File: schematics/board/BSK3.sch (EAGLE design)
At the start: 44 parts

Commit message: Изменены площадки для сплавов Розе
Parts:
- U$15, U$16, U$6, U$7: value GRAFITGRAFIT3_1 -> GRAFITGRAFIT4_2; device CanCubeSat:GRAFITGRAFIT3_1 -> CanCubeSat:GRAFITGRAFIT4_2
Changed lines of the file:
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@@
 <part name="LED7" library="led" library_urn="urn:adsk.eagle:library:259" deviceset="LED" device="CHIPLED_0603" package3d_urn="urn:adsk.eagle:package:15822/2"/>
 <part name="R14" library="resistor" library_urn="urn:adsk.eagle:library:348" deviceset="R-US_" device="R0603" package3d_urn="urn:adsk.eagle:package:23555/3" value="1M"/>
-<part name="U$6" library="CanCubeSat" deviceset="GRAFIT" device="GRAFIT3_1"/>
-<part name="U$7" library="CanCubeSat" deviceset="GRAFIT" device="GRAFIT3_1"/>
-<part name="U$15" library="CanCubeSat" deviceset="GRAFIT" device="GRAFIT3_1"/>
-<part name="U$16" library="CanCubeSat" deviceset="GRAFIT" device="GRAFIT3_1"/>
+<part name="U$6" library="CanCubeSat" deviceset="GRAFIT" device="GRAFIT4_2" value="GRAFITGRAFIT4_2"/>
+<part name="U$7" library="CanCubeSat" deviceset="GRAFIT" device="GRAFIT4_2" value="GRAFITGRAFIT4_2"/>
+<part name="U$15" library="CanCubeSat" deviceset="GRAFIT" device="GRAFIT4_2" value="GRAFITGRAFIT4_2"/>
+<part name="U$16" library="CanCubeSat" deviceset="GRAFIT" device="GRAFIT4_2" value="GRAFITGRAFIT4_2"/>
 <part name="R75" library="rcl" library_urn="urn:adsk.eagle:library:334" deviceset="R-US_" device="R2512" package3d_urn="urn:adsk.eagle:package:23545/2" value="R01"/>
 <part name="R76" library="resistor" deviceset="R-US_" device="R0603" package3d_urn="urn:adsk.eagle:package:23555/3" value="10R"/>

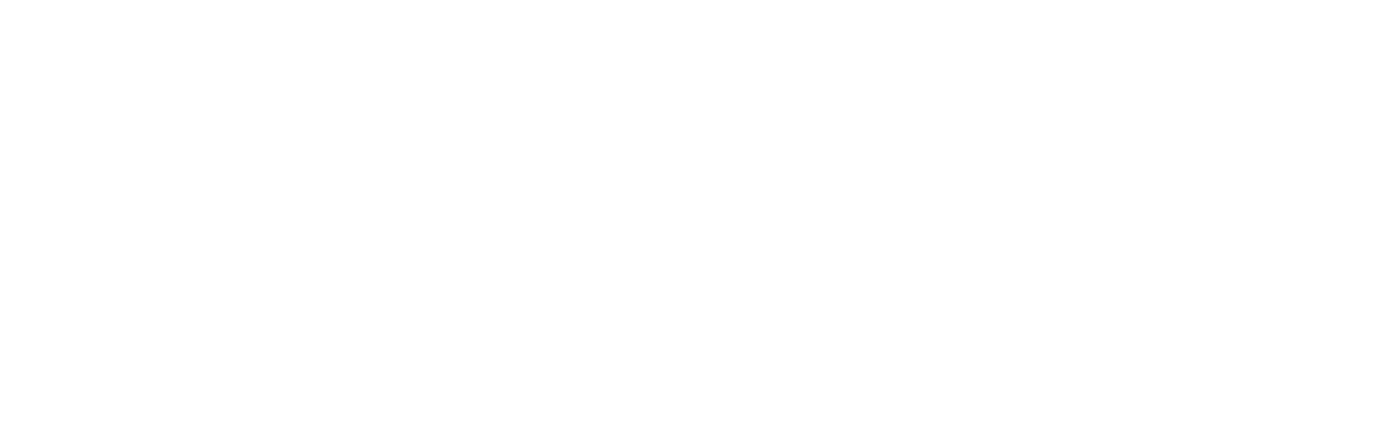
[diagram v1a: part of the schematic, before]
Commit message: Добавлены подписи Концерна к платам
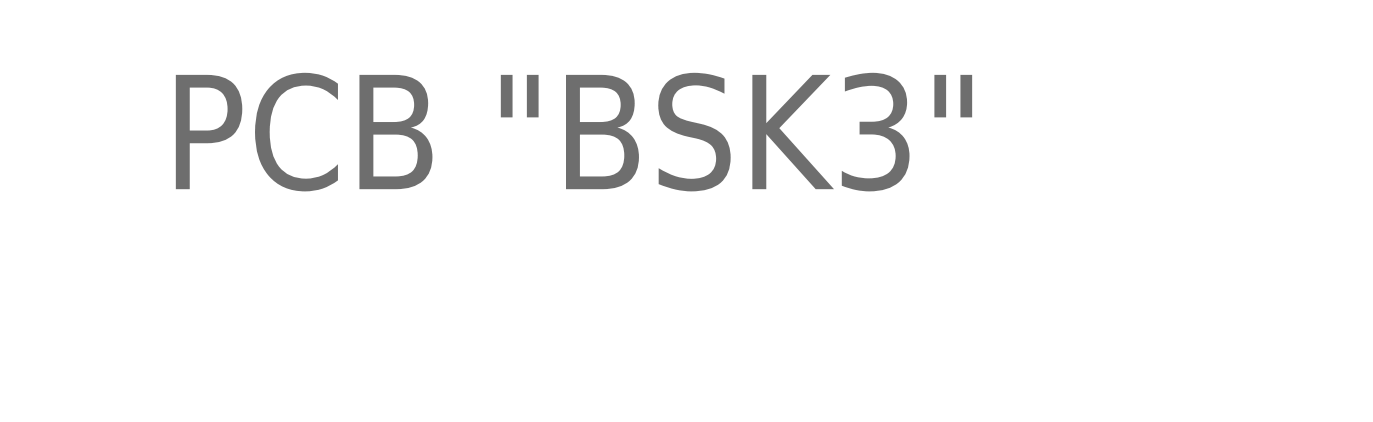
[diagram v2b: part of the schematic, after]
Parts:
- added U$9: PCB "BSK3", CanCubeSat:ITS-LOGOPCB-""
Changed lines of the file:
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@@
 <drawing>
 <settings>
-<setting alwaysvectorfont="no"/>
+<setting alwaysvectorfont="yes"/>
 <setting verticaltext="up"/>
 </settings>
@@
 <part name="R32" library="resistor" deviceset="R-US_" device="R0603" package3d_urn="urn:adsk.eagle:package:23555/3" value="100R"/>
 <part name="R3" library="resistor" deviceset="R-US_" device="R0603" package3d_urn="urn:adsk.eagle:package:23555/3" value="100R"/>
+<part name="U$9" library="CanCubeSat" deviceset="ITS-LOGO" device="PCB-&quot;&quot;" value="PCB &quot;BSK3&quot;"/>
 </parts>
 <sheets>
@@
 <attribute name="VALUE" x="173.482" y="39.37" size="1.778" layer="96" rot="R90"/>
 </instance>
+<instance part="U$9" gate="G$1" x="109.22" y="304.8" smashed="yes">
+<attribute name="VALUE" x="236.22" y="304.8" size="12.7" layer="96"/>
+</instance>
 </instances>

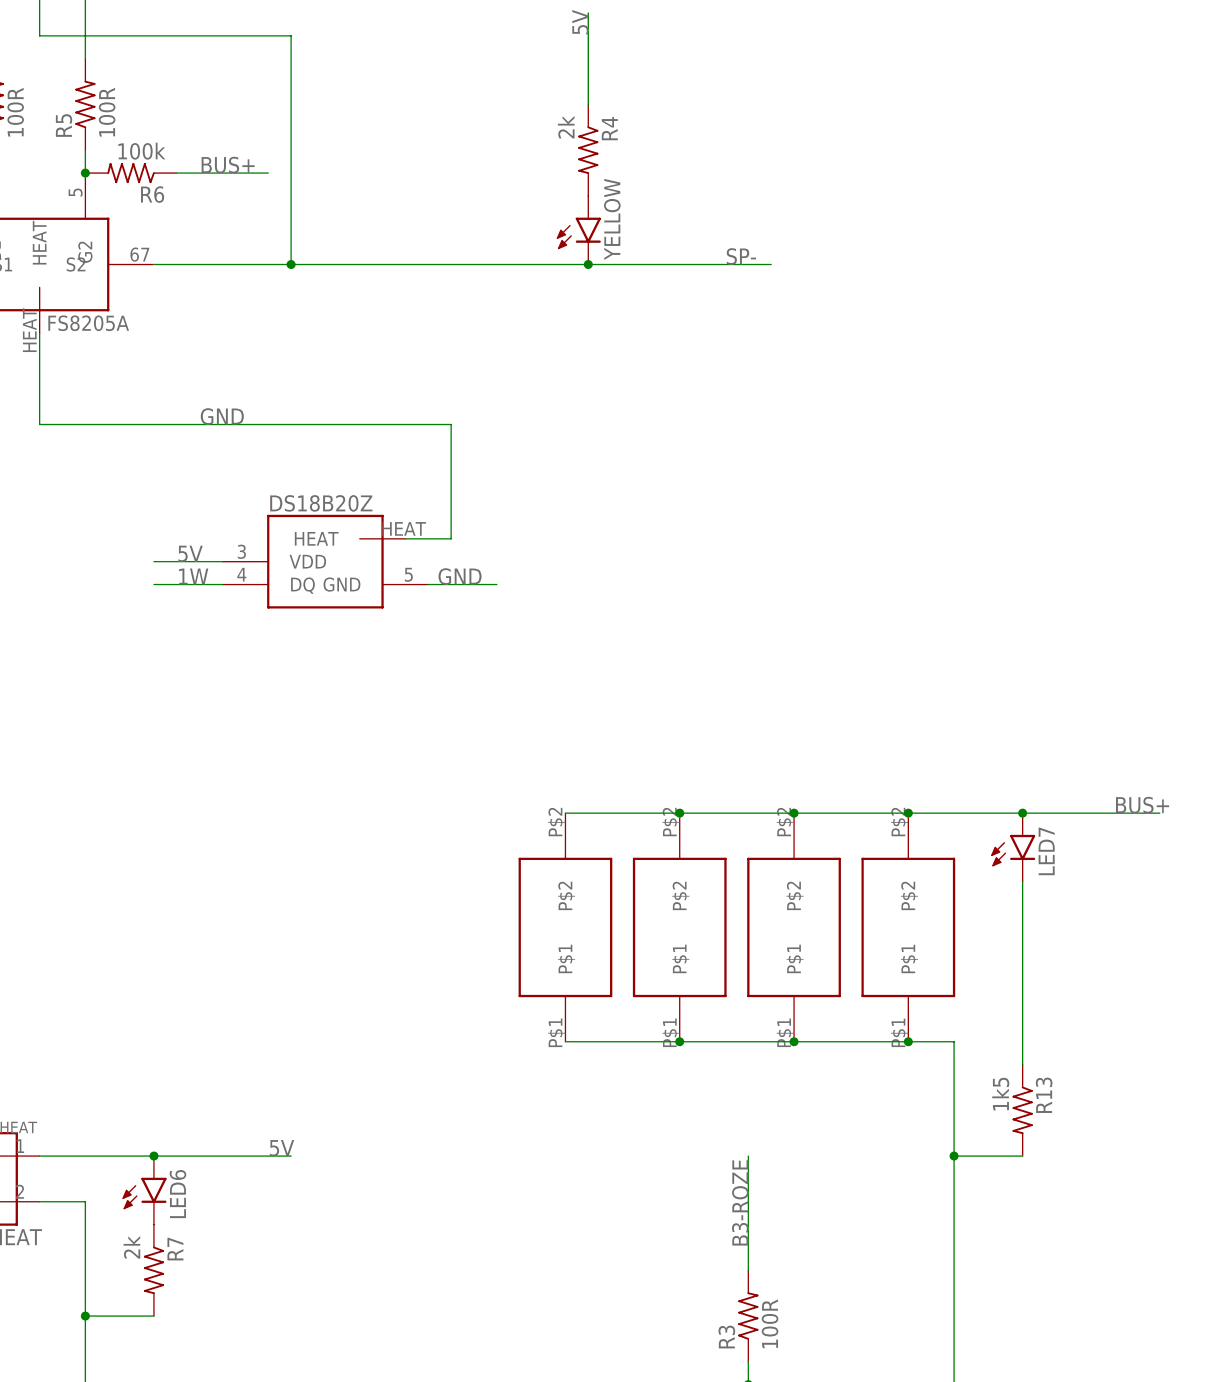
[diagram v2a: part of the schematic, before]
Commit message: Добавлена шелкография на платах БСК и СП
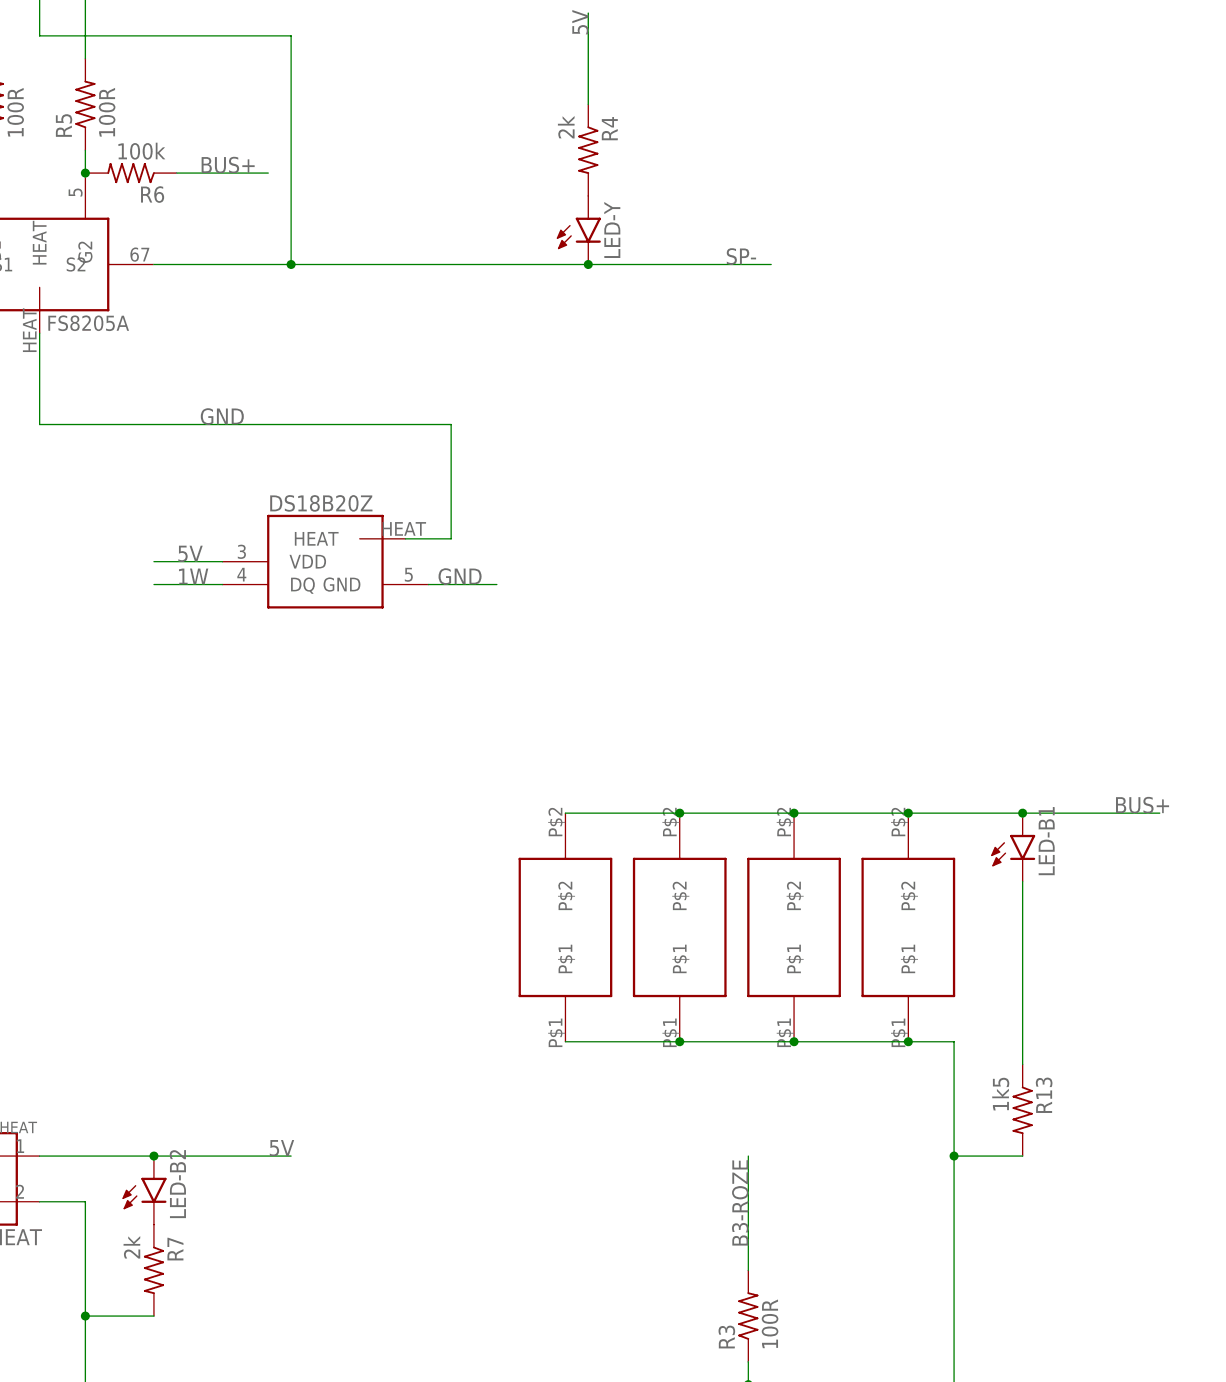
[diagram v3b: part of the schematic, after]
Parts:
- U$5: value MOCD217M -> MOCD
- renumbered DS18B20Z1 to DS18B20Z, LED6 to LED-B2, LED7 to LED-B1, U$57 to INA, YELLOW to LED-Y
